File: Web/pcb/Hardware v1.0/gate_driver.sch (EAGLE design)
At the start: 25 parts, among them IC1 HCPL3120, IC2 HCPL3120

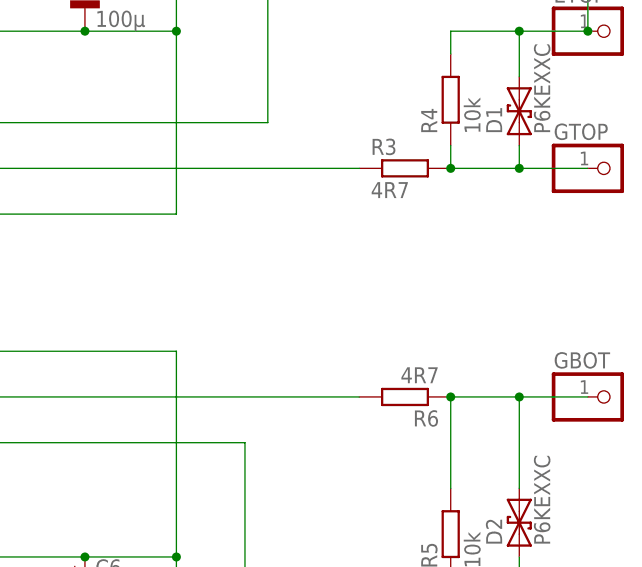
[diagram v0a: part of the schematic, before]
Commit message: converted updater to php
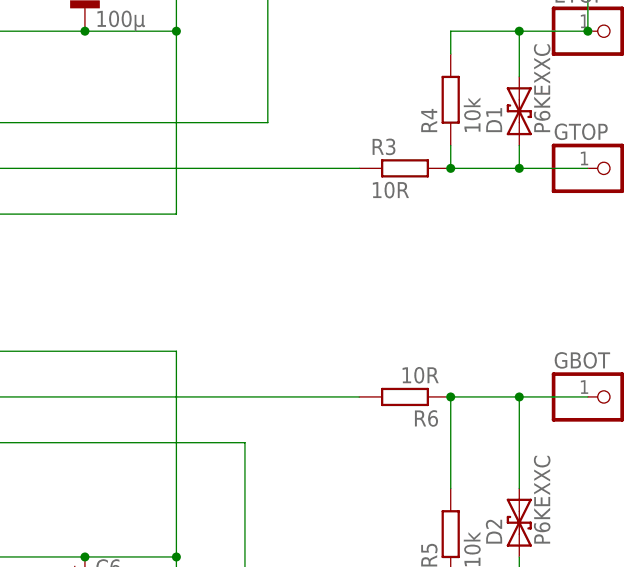
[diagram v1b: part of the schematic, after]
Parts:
- R3, R6: value 4R7 -> 10R
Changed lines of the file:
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@@
 <?xml version="1.0" encoding="utf-8"?>
 <!DOCTYPE eagle SYSTEM "eagle.dtd">
-<eagle version="8.0.1">
+<eagle version="8.1.1">
 <drawing>
 <settings>
@@
 <part name="GBOT" library="pinhead" deviceset="PINHD-1X1" device=""/>
 <part name="EBOT" library="pinhead" deviceset="PINHD-1X1" device=""/>
-<part name="R3" library="rcl" deviceset="R-EU_" device="0309/12" value="4R7"/>
+<part name="R3" library="rcl" deviceset="R-EU_" device="0309/12" value="10R"/>
 <part name="R4" library="rcl" deviceset="R-EU_" device="0207/10" value="10k"/>
 <part name="R5" library="rcl" deviceset="R-EU_" device="0207/10" value="10k"/>
-<part name="R6" library="rcl" deviceset="R-EU_" device="0309/12" value="4R7"/>
+<part name="R6" library="rcl" deviceset="R-EU_" device="0309/12" value="10R"/>
 <part name="-_BT_TP_+" library="pinhead" deviceset="PINHD-1X4" device=""/>
 <part name="C7" library="rcl" deviceset="CPOL-EU" device="E2.5-5" value="100µ"/>
